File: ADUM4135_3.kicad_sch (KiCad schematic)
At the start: 36 parts, among them Q10 MJD45H11T4G, Q11 MJD44H11T4G, Q12 MJD45H11T4G, Q9 MJD44H11T4G

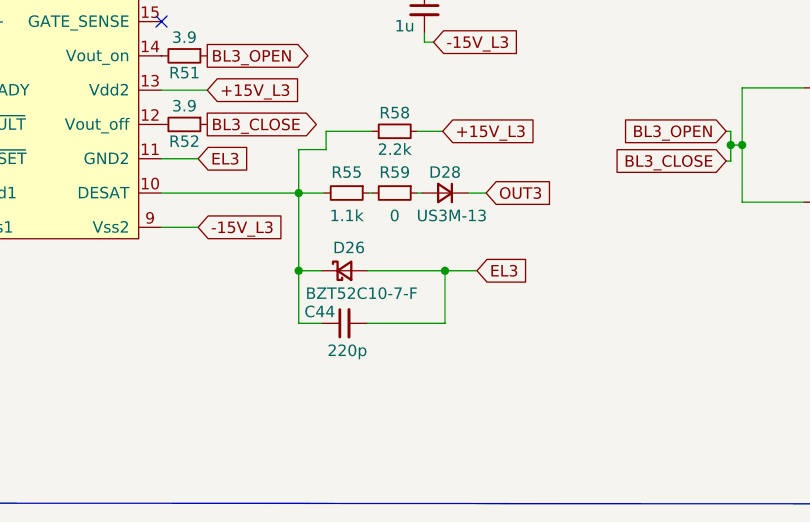
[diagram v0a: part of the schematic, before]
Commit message: Добавил названия элементов в схеме
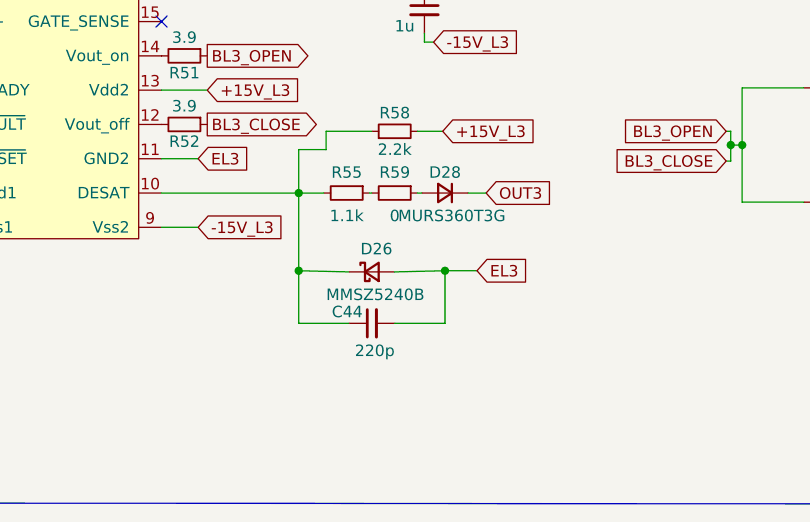
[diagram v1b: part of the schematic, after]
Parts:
- D25, D26: value BZT52C10-7-F -> MMSZ5240B
- D27, D28: value US3M-13 -> MURS360T3G
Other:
- moved on the sheet: C44, D26
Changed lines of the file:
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@@
     (stroke (width 0) (type default) (color 0 0 0 0))
   )
-  (wire (pts (xy 112.522 155.448) (xy 109.982 155.448))
+  (wire (pts (xy 115.57 155.575) (xy 109.982 155.448))
     (stroke (width 0) (type default) (color 0 0 0 0))
   )
@@
     (stroke (width 0) (type default) (color 0 0 0 0))
   )
-  (wire (pts (xy 117.602 155.448) (xy 126.238 155.448))
+  (wire (pts (xy 120.65 155.575) (xy 126.238 155.448))
     (stroke (width 0) (type default) (color 0 0 0 0))
   )
@@
     (stroke (width 0) (type default) (color 0 0 0 0))
   )
-  (wire (pts (xy 112.522 161.29) (xy 109.982 161.29))
+  (wire (pts (xy 115.57 161.29) (xy 109.982 161.29))
     (stroke (width 0) (type default) (color 0 0 0 0))
   )
@@
     (stroke (width 0) (type default) (color 0 0 0 0))
   )
-  (wire (pts (xy 117.602 161.29) (xy 126.238 161.29))
+  (wire (pts (xy 120.65 161.29) (xy 126.238 161.29))
     (stroke (width 0) (type default) (color 0 0 0 0))
   )
@@
     (in_bom yes) (on_board yes)
     (property "Reference" "D28" (id 0) (at 126.238 144.526 0))
-    (property "Value" "US3M-13" (id 1) (at 127 149.352 0))
+    (property "Value" "MURS360T3G" (id 1) (at 127 149.352 0))
     (property "Footprint" "Diode_SMD:D_SMC" (id 2) (at 126.238 146.812 90)
       (effects (font (size 1.27 1.27)) hide)
@@
       (effects (font (size 1.27 1.27)) (justify left))
     )
-    (property "Value" "BZT52C10-7-F" (id 1) (at 111.252 78.994 90)
+    (property "Value" "MMSZ5240B" (id 1) (at 111.252 78.994 90)
       (effects (font (size 1.27 1.27)) (justify left) hide)
     )
@@
     (pin "4")
   )
-  (symbol (lib_id "Device:C_Small") (at 115.062 161.29 90) (unit 1)
-    (in_bom yes) (on_board yes)
-    (property "Reference" "C44" (id 0) (at 114.046 160.02 90)
-      (effects (font (size 1.27 1.27)) (justify left))
-    )
-    (property "Value" "220p" (id 1) (at 117.602 164.338 90)
-      (effects (font (size 1.27 1.27)) (justify left))
-    )
-    (property "Footprint" "Capacitor_SMD:C_0805_2012Metric_Pad1.18x1.45mm_HandSolder" (id 2) (at 115.062 161.29 0)
-      (effects (font (size 1.27 1.27)) hide)
-    )
-    (property "Datasheet" "~" (id 3) (at 115.062 161.29 0)
+  (symbol (lib_id "Device:C_Small") (at 118.11 161.29 90) (unit 1)
+    (in_bom yes) (on_board yes)
+    (property "Reference" "C44" (id 0) (at 117.094 160.02 90)
+      (effects (font (size 1.27 1.27)) (justify left))
+    )
+    (property "Value" "220p" (id 1) (at 120.65 164.338 90)
+      (effects (font (size 1.27 1.27)) (justify left))
+    )
+    (property "Footprint" "Capacitor_SMD:C_0805_2012Metric_Pad1.18x1.45mm_HandSolder" (id 2) (at 118.11 161.29 0)
+      (effects (font (size 1.27 1.27)) hide)
+    )
+    (property "Datasheet" "~" (id 3) (at 118.11 161.29 0)
       (effects (font (size 1.27 1.27)) hide)
     )
@@
     (in_bom yes) (on_board yes)
     (property "Reference" "D27" (id 0) (at 119.888 78.994 90))
-    (property "Value" "US3M-13" (id 1) (at 115.062 79.756 0)
+    (property "Value" "MURS360T3G" (id 1) (at 115.062 79.756 0)
       (effects (font (size 1.27 1.27)) hide)
     )
@@
     (pin "1")
   )
-  (symbol (lib_id "Device:D_Schottky_Small") (at 115.062 155.448 0) (unit 1)
-    (in_bom yes) (on_board yes)
-    (property "Reference" "D26" (id 0) (at 113.792 152.908 0)
-      (effects (font (size 1.27 1.27)) (justify left))
-    )
-    (property "Value" "BZT52C10-7-F" (id 1) (at 110.744 157.988 0)
-      (effects (font (size 1.27 1.27)) (justify left))
-    )
-    (property "Footprint" "Diode_SMD:D_SOD-123" (id 2) (at 115.062 155.448 90)
-      (effects (font (size 1.27 1.27)) hide)
-    )
-    (property "Datasheet" "~" (id 3) (at 115.062 155.448 90)
-      (effects (font (size 1.27 1.27)) hide)
-    )
+  (symbol (lib_id "Device:D_Schottky_Small") (at 118.11 155.575 0) (unit 1)
+    (in_bom yes) (on_board yes)
+    (property "Reference" "D26" (id 0) (at 116.84 153.035 0)
+      (effects (font (size 1.27 1.27)) (justify left))
+    )
+    (property "Value" "MMSZ5240B" (id 1) (at 113.03 158.115 0)
+      (effects (font (size 1.27 1.27)) (justify left))
+    )
+    (property "Footprint" "Diode_SMD:D_SOD-123" (id 2) (at 118.11 155.575 90)
+      (effects (font (size 1.27 1.27)) hide)
+    )
+    (property "Datasheet" "~" (id 3) (at 118.11 155.575 90)
+      (effects (font (size 1.27 1.27)) hide)
+    )

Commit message: Нашёл ошибки
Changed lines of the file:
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@@
     (stroke (width 0) (type default) (color 0 0 0 0))
   )
-  (wire (pts (xy 115.57 155.575) (xy 109.982 155.448))
+  (wire (pts (xy 115.57 155.448) (xy 109.982 155.448))
     (stroke (width 0) (type default) (color 0 0 0 0))
   )
@@
     (stroke (width 0) (type default) (color 0 0 0 0))
   )
-  (wire (pts (xy 120.65 155.575) (xy 126.238 155.448))
+  (wire (pts (xy 120.65 155.448) (xy 126.238 155.448))
     (stroke (width 0) (type default) (color 0 0 0 0))
   )
@@
     (pin "1")
   )
-  (symbol (lib_id "Device:D_Schottky_Small") (at 118.11 155.575 0) (unit 1)
-    (in_bom yes) (on_board yes)
-    (property "Reference" "D26" (id 0) (at 116.84 153.035 0)
-      (effects (font (size 1.27 1.27)) (justify left))
-    )
-    (property "Value" "MMSZ5240B" (id 1) (at 113.03 158.115 0)
-      (effects (font (size 1.27 1.27)) (justify left))
-    )
-    (property "Footprint" "Diode_SMD:D_SOD-123" (id 2) (at 118.11 155.575 90)
-      (effects (font (size 1.27 1.27)) hide)
-    )
-    (property "Datasheet" "~" (id 3) (at 118.11 155.575 90)
-      (effects (font (size 1.27 1.27)) hide)
-    )
+  (symbol (lib_id "Device:D_Schottky_Small") (at 118.11 155.448 0) (unit 1)
+    (in_bom yes) (on_board yes)
+    (property "Reference" "D26" (id 0) (at 116.84 152.908 0)
+      (effects (font (size 1.27 1.27)) (justify left))
+    )
+    (property "Value" "MMSZ5240B" (id 1) (at 113.03 157.988 0)
+      (effects (font (size 1.27 1.27)) (justify left))
+    )
+    (property "Footprint" "Diode_SMD:D_SOD-123" (id 2) (at 118.11 155.448 90)
+      (effects (font (size 1.27 1.27)) hide)
+    )
+    (property "Datasheet" "~" (id 3) (at 118.11 155.448 90)
+      (effects (font (size 1.27 1.27)) hide)
+    )
